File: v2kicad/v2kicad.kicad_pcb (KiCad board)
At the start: 2 copper layers, 72 x 59 mm, 4 parts

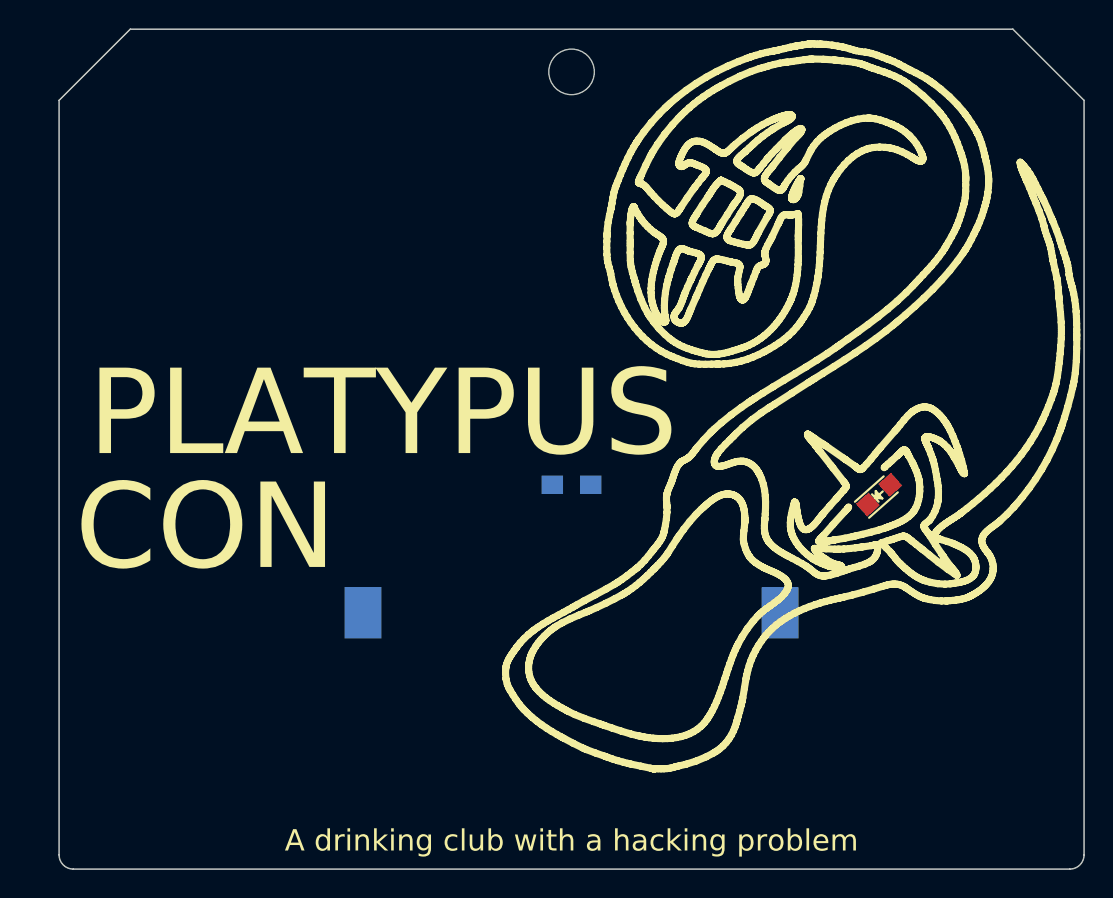
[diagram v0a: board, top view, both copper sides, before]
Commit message: Redone traces for main LED to avoid silkscreen
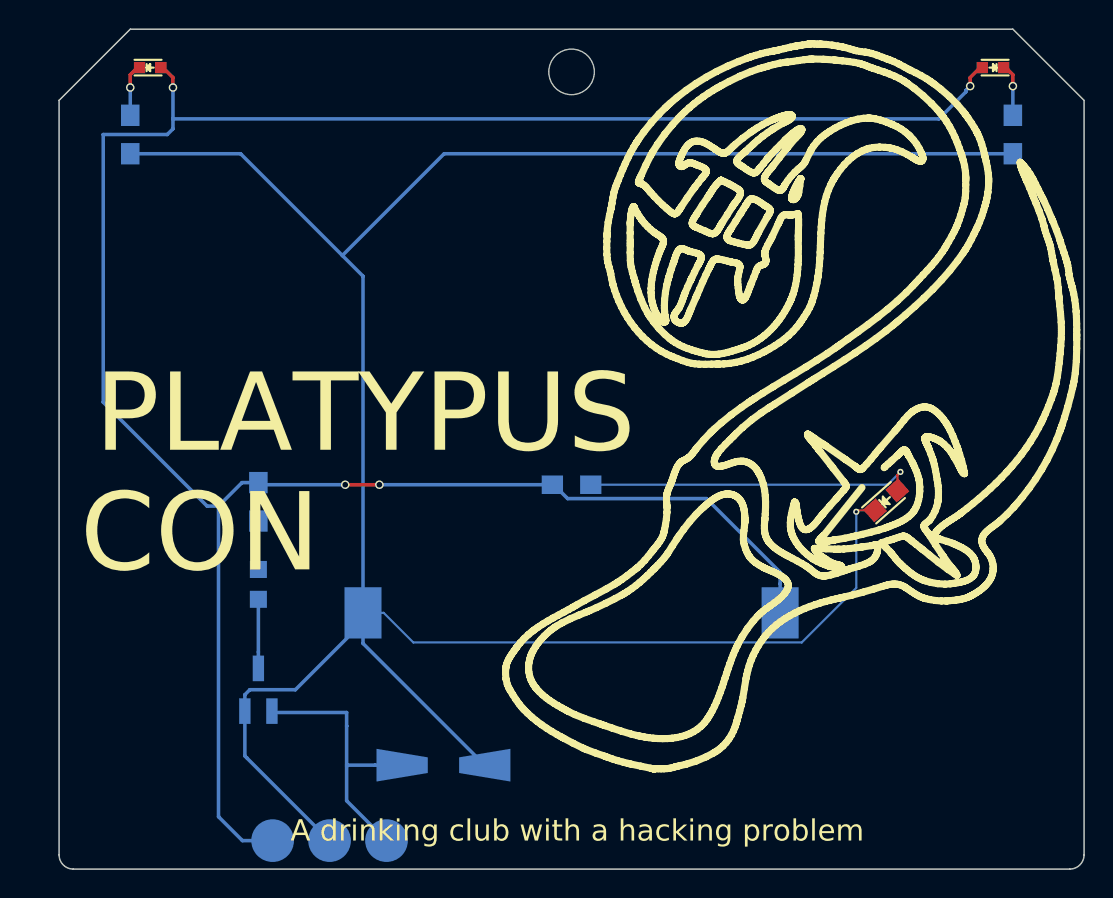
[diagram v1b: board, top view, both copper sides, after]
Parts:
- added D2: ZENERsmall, Diodes_SMD:SMA-SMB_Universal_Handsoldering, B.Cu at (154.0, 126.7)
- added D3: LED, LEDs:LED_0805, B.Cu at (141.0, 114.0)
- added D4: LED, LEDs:LED_0603, F.Cu at (133.4, 77.7)
- added D5: LED, LEDs:LED_0603, F.Cu at (192.6, 77.7)
- added P1: CONN_01X01, Measurement_Points:Measurement_Point_Round-SMD-Pad_Big, B.Cu at (150.0, 132.0)
- added P2: CONN_01X01, Measurement_Points:Measurement_Point_Round-SMD-Pad_Big, B.Cu at (146.0, 132.0)
- added P3: CONN_01X01, Measurement_Points:Measurement_Point_Round-SMD-Pad_Big, B.Cu at (142.0, 132.0)
- added Q1: Q_NMOS_GSD, TO_SOT_Packages_SMD:SOT-23_Handsoldering, B.Cu at (141.0, 121.4)
- added R2: R, Resistors_SMD:R_0805_HandSoldering, B.Cu at (141.0, 108.2)
- added R3: R, Resistors_SMD:R_0805_HandSoldering, B.Cu at (132.0, 82.4)
- added R4: R, Resistors_SMD:R_0805_HandSoldering, B.Cu at (194.0, 82.4)
- moved D1 0.64 mm to (185.1, 108.1)
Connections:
- net Net-(BT1-Pad1) renamed +3V3
- net Net-(BT1-Pad2) renamed GND
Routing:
- net GND: track 0.00 -> 175.4 mm, vias 0 -> 1
- net +3V3: track 0.00 -> 170.4 mm, vias 0 -> 4
- net Net-(D1-Pad2): track 0.00 -> 23.5 mm, vias 0 -> 1
- net Net-(D2-Pad1): track 0.00 -> 19.3 mm
- net Net-(D3-Pad1): track 0.00 -> 4.85 mm
- net Net-(D5-Pad1): track 0.00 -> 3.71 mm, vias 0 -> 1
- net Net-(D4-Pad1): track 0.00 -> 3.71 mm, vias 0 -> 1
- net Net-(D3-Pad2): track 0.00 -> 3.40 mm
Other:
- rule trace_min: 0.2 -> 0.15
- rule via_min_drill: 0.3 -> 0.22
- rule via_min_size: 0.4 -> 0.44
